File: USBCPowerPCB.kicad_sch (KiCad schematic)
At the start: 3 parts, among them J2 USB_C_Receptacle_USB2.0_16P

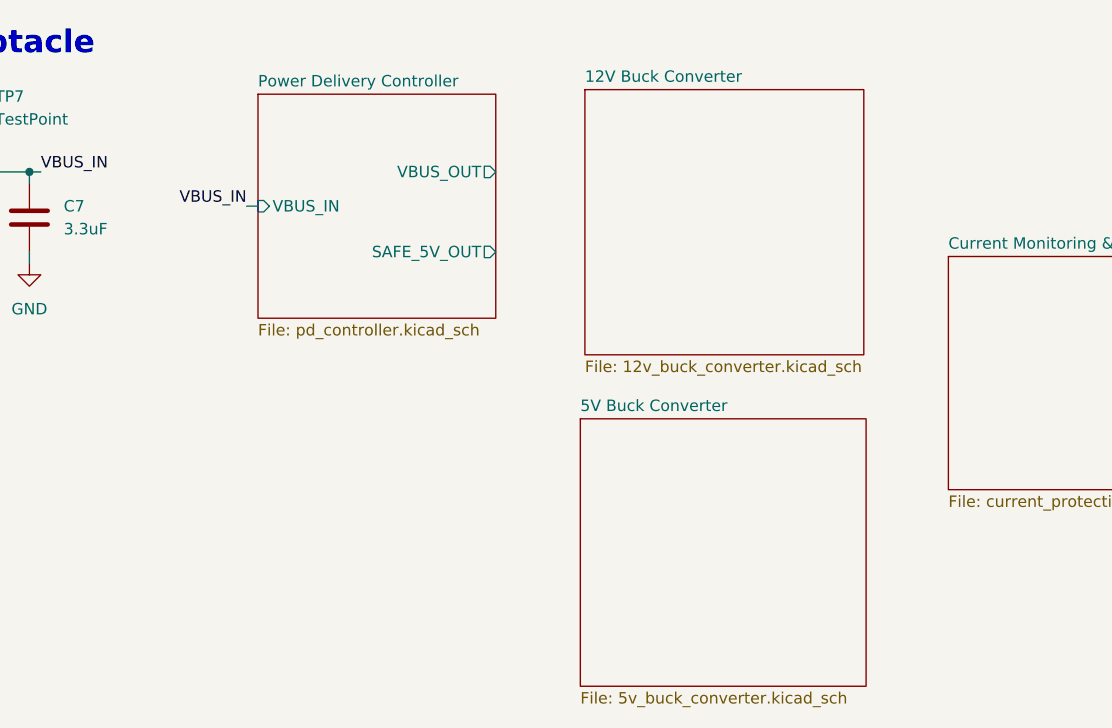
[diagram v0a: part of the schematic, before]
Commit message: Finished 5V buck converter schematic
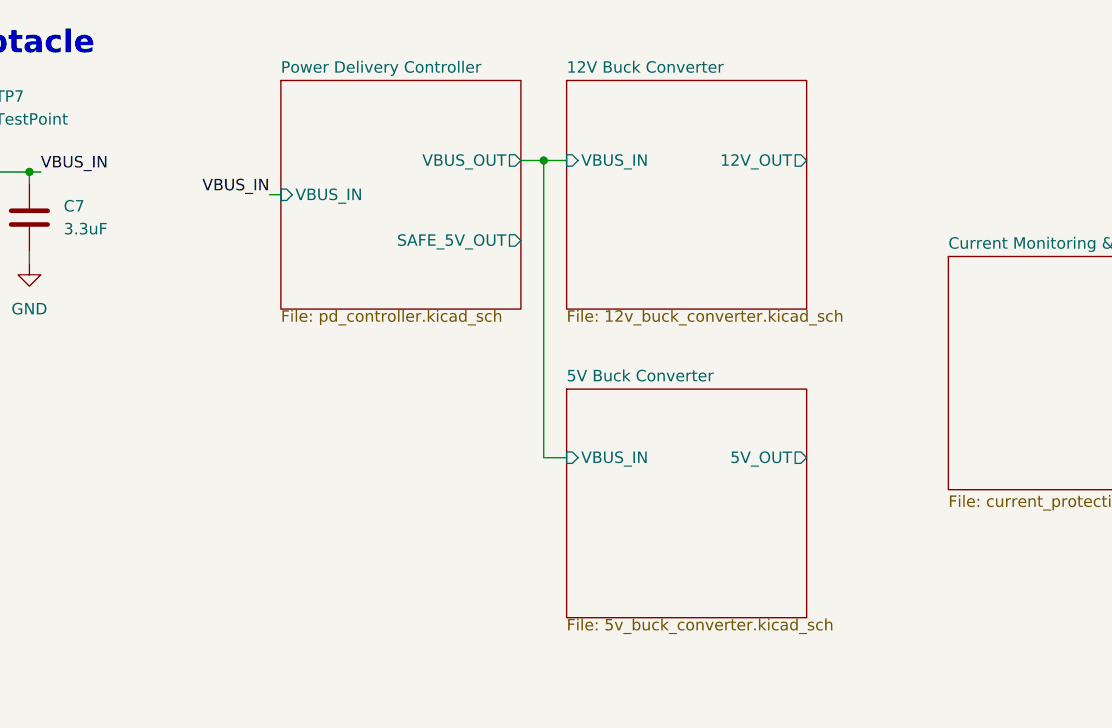
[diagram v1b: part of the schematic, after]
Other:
- sheet 12V Buck Converter ports: added 12V_OUT, VBUS_IN; removed none
- sheet 5V Buck Converter ports: added 5V_OUT, VBUS_IN; removed none
- company: (none) -> Longhorn Racing Solar
- title: (none) -> USB Type-C Power Distribution Board
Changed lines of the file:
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@@
 	(generator_version "8.0")
 	(paper "A4")
+	(title_block
+		(title "USB Type-C Power Distribution Board")
+		(company "Longhorn Racing Solar")
+		(comment 1 "https://cloud.wikis.utexas.edu/wiki/x/-qKvAQ")
+	)
+	(junction
+		(at 120.65 36.83)
+		(diameter 0)
+		(color 0 0 0 0)
+	)
 	(junction
 		(at 57.15 38.1)
@@
 	(wire
 		(pts
+			(xy 120.65 36.83) (xy 123.19 36.83)
+		)
+		(stroke
+			(width 0)
+			(type default)
+		)
+	)
+	(wire
+		(pts
 			(xy 38.1 76.2) (xy 38.1 78.74)
 		)
@@
 	(wire
 		(pts
+			(xy 123.19 69.85) (xy 120.65 69.85)
+		)
+		(stroke
+			(width 0)
+			(type default)
+		)
+	)
+	(wire
+		(pts
 			(xy 57.15 34.29) (xy 57.15 38.1)
 		)
@@
 	(wire
 		(pts
+			(xy 120.65 69.85) (xy 120.65 36.83)
+		)
+		(stroke
+			(width 0)
+			(type default)
+		)
+	)
+	(wire
+		(pts
 			(xy 63.5 38.1) (xy 64.77 38.1)
 		)
@@
 	(wire
 		(pts
-			(xy 87.63 41.91) (xy 88.9 41.91)
+			(xy 90.17 40.64) (xy 91.44 40.64)
+		)
+		(stroke
+			(width 0)
+			(type default)
+		)
+	)
+	(wire
+		(pts
+			(xy 118.11 36.83) (xy 120.65 36.83)
 		)
 		(stroke
@@
 	)
 	(label "VBUS_IN"
-		(at 87.63 41.91 180)
+		(at 90.17 40.64 180)
 		(fields_autoplaced yes)
 		(effects
@@
 			(project "USBCPowerPCB"
 				(path "/f58400c5-df4b-4929-8d2b-33c0fe23fcd9"
-					(page "4")
+					(page "5")
 				)
 			)
@@
 	)
 	(sheet
-		(at 124.714 65.532)
-		(size 31.75 29.718)
+		(at 123.19 62.23)
+		(size 26.67 25.4)
 		(fields_autoplaced yes)
 		(stroke
@@
 		)
 		(property "Sheetname" "5V Buck Converter"
-			(at 124.714 64.8204 0)
+			(at 123.19 61.5184 0)
 			(effects
 				(font
@@
 		)
 		(property "Sheetfile" "5v_buck_converter.kicad_sch"
-			(at 124.714 95.8346 0)
+			(at 123.19 87.7066 0)
 			(effects
 				(font
@@
 				)
 				(justify left top)
+			)
+		)
+		(pin "VBUS_IN" input
+			(at 123.19 69.85 180)
+			(effects
+				(font
+					(size 1.27 1.27)
+				)
+				(justify left)
+			)
+		)
+		(pin "5V_OUT" output
+			(at 149.86 69.85 0)
+			(effects
+				(font
+					(size 1.27 1.27)
+				)
+				(justify right)
 			)
 		)
@@
 			(project "USBCPowerPCB"
 				(path "/f58400c5-df4b-4929-8d2b-33c0fe23fcd9"
-					(page "5")
+					(page "4")
 				)
 			)
@@
 	)
 	(sheet
-		(at 88.9 29.464)
-		(size 26.416 24.892)
+		(at 91.44 27.94)
+		(size 26.67 25.4)
 		(fields_autoplaced yes)
 		(stroke
@@
 		)
 		(property "Sheetname" "Power Delivery Controller"
-			(at 88.9 28.7524 0)
+			(at 91.44 27.2284 0)
 			(effects
 				(font
@@
 		)
 		(property "Sheetfile" "pd_controller.kicad_sch"
-			(at 88.9 54.9406 0)
+			(at 91.44 53.4166 0)
 			(effects
 				(font
@@
 		)
 		(pin "VBUS_IN" input
-			(at 88.9 41.91 180)
+			(at 91.44 40.64 180)
 			(effects
 				(font
@@
 		)
 		(pin "VBUS_OUT" output
-			(at 115.316 38.1 0)
+			(at 118.11 36.83 0)
 			(effects
 				(font
@@
 		)
 		(pin "SAFE_5V_OUT" output
-			(at 115.316 46.99 0)
+			(at 118.11 45.72 0)
 			(effects
 				(font
@@
 	)
 	(sheet
-		(at 125.222 28.956)
-		(size 30.988 29.464)
+		(at 123.19 27.94)
+		(size 26.67 25.4)
 		(fields_autoplaced yes)
 		(stroke
@@
 		)
 		(property "Sheetname" "12V Buck Converter"
-			(at 125.222 28.2444 0)
+			(at 123.19 27.2284 0)
 			(effects
 				(font
@@
 		)
 		(property "Sheetfile" "12v_buck_converter.kicad_sch"
-			(at 125.222 59.0046 0)
+			(at 123.19 53.4166 0)
 			(effects
 				(font
@@
 			)
 		)
+		(pin "VBUS_IN" input
+			(at 123.19 36.83 180)
+			(effects
+				(font
+					(size 1.27 1.27)
+				)
+				(justify left)
+			)
+		)
+		(pin "12V_OUT" output
+			(at 149.86 36.83 0)
+			(effects
+				(font
+					(size 1.27 1.27)
+				)
+				(justify right)
+			)
+		)

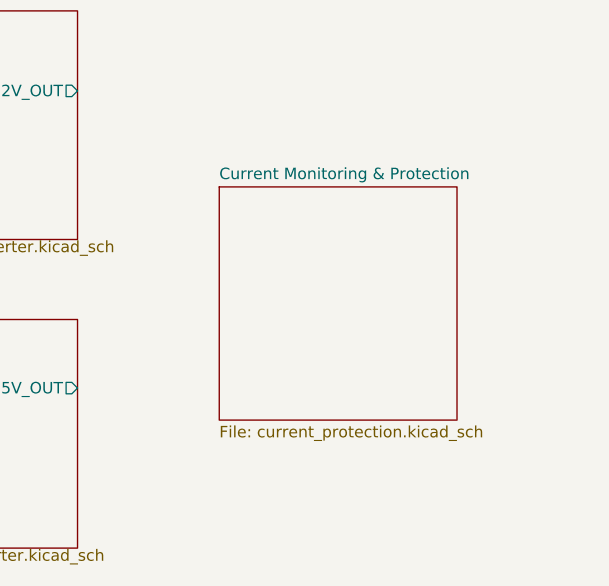
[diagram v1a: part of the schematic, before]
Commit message: change current protection to current monitoring
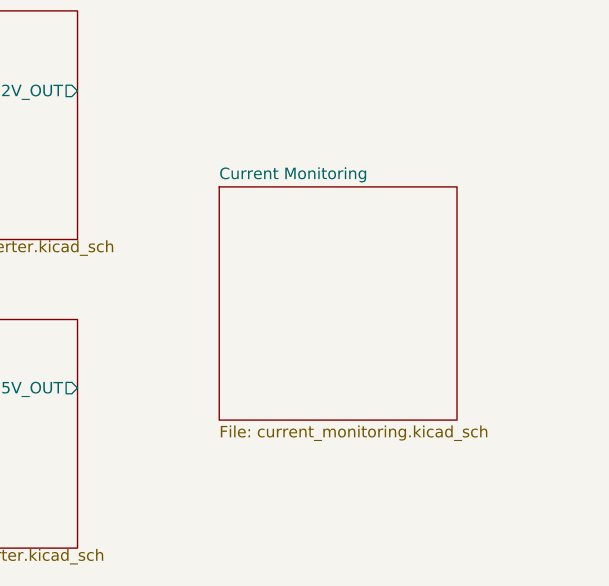
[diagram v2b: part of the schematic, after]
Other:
- sheet Current Monitoring & Protection renamed Current Monitoring
- sheet Current Monitoring: file current_protection.kicad_sch -> current_monitoring.kicad_sch
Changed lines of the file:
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@@
 			(color 0 0 0 0.0000)
 		)
-		(property "Sheetname" "Current Monitoring & Protection"
+		(property "Sheetname" "Current Monitoring"
 			(at 165.608 46.7864 0)
 			(effects
@@
 			)
 		)
-		(property "Sheetfile" "current_protection.kicad_sch"
+		(property "Sheetfile" "current_monitoring.kicad_sch"
 			(at 165.608 73.9906 0)
 			(effects

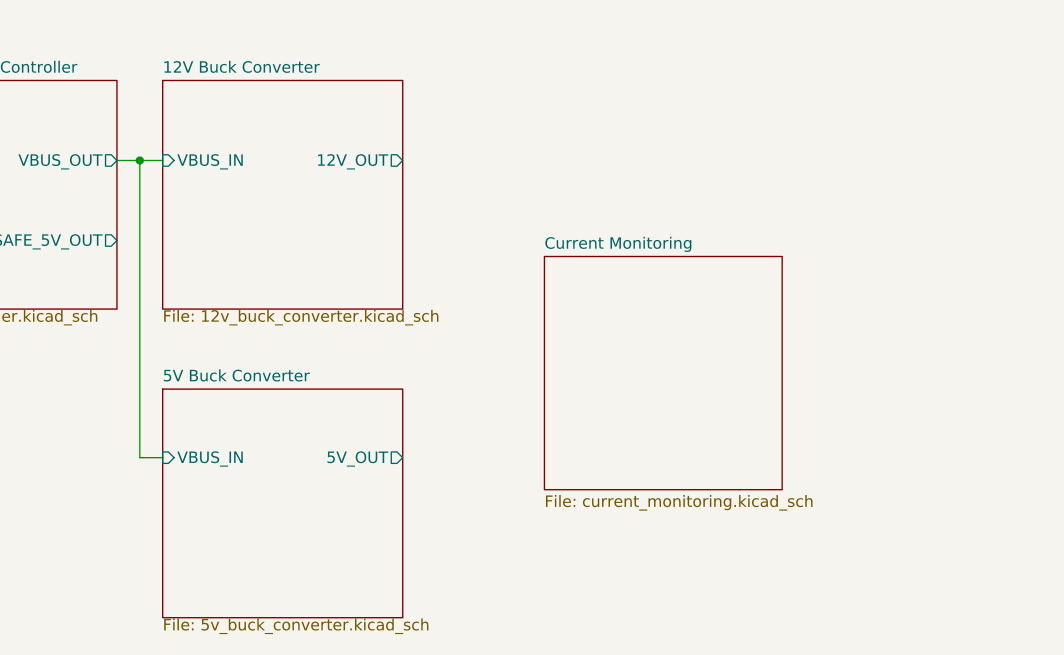
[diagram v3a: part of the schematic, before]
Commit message: accidentally flipped current sense; also routed high level schematic
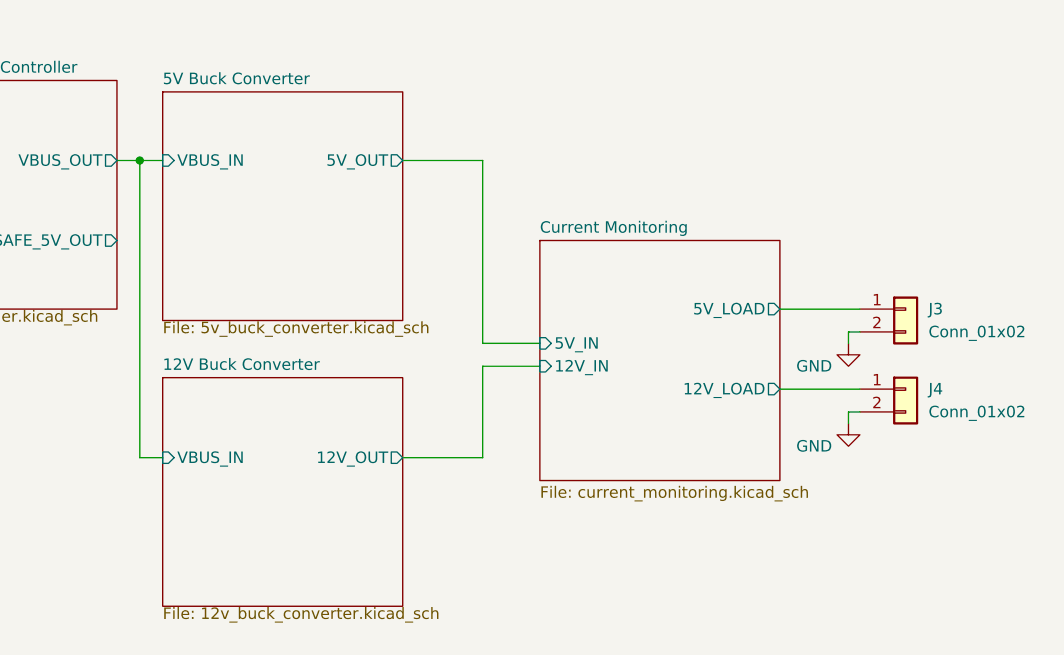
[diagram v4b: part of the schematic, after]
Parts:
- added J3, J4: Conn_01x02, symbol Connector_Generic:Conn_01x02
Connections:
- net GND: now also J3.2 (Pin_2), J4.2 (Pin_2)
- new net Current Monitoring/12V_LOAD: J4.1 (Pin_1)
- new net Current Monitoring/5V_LOAD: J3.1 (Pin_1)
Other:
- sheet Current Monitoring ports: added 12V_IN, 12V_LOAD, 5V_IN, 5V_LOAD; removed none

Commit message: finished first draft
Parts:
- J3: value Conn_01x02 -> 5V_OUT
- J4: value Conn_01x02 -> 12V_OUT
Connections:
- net VBUS_IN renamed Power Delivery Controller/VBUS_IN
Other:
- note added: "USB Type-C Power Supply PCB"
- moved on the sheet: C7, J2, J3, J4, TP7
